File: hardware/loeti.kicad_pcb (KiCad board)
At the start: 2 copper layers, 69.3 x 41.9 mm, 64 parts, among them J1 GCT USB4105, J2 AudioJack3, J3 20021112-00014T1LF, Q1 BC817, Q2 BC817, Q3 BC807, Q4 Si4825DDY, DMG4435SSS, IRF939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, SW1 D6R, U1 STUSB4500QTR, U2 AP2204R-3.3, U3 STM32F030K6Tx, U4 74AHC1G08, U5 INA301, U6 TMP100, U7 TLV333-DBV

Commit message: two-temperature mode
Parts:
- removed D7: LED, LED_THT:LED_D1.8mm_W3.3mm_H2.4mm
- removed R12: 10k, Resistor_SMD:R_0603_1608Metric_Pad0.98x0.95mm_HandSolder
- C12, C13: value 100n -> DNP
- R10, R11, R18: value 10k -> 1k
- R13: value 1k -> 10k
- moved D6 7.04 mm to (83.0, -40.5), turned to 0 degrees
- moved D5 5.66 mm to (83.0, -43.5), turned to 0 degrees
- moved R11 5.64 mm to (84.0, -47.5), turned to 180 degrees
- moved R10 4.80 mm to (84.0, -45.8), turned to 180 degrees
- moved R3 1.25 mm to (84.5, -37.8), turned to 0 degrees
- moved R1 1.00 mm to (78.8, -39.5)
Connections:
- D5 pad 1: HEATER- -> Net-(D5-Pad1)
- D5 pad 2: Net-(D5-Pad2) -> LED0
- D6 pad 1: HEATER- -> Net-(D6-Pad1)
- D6 pad 2: Net-(D6-Pad2) -> LED1
- R10 pad 1: Net-(D5-Pad2) -> HEATER-
- R10 pad 2: LED0 -> Net-(D5-Pad1)
- R11 pad 1: Net-(D6-Pad2) -> HEATER-
- R11 pad 2: LED1 -> Net-(D6-Pad1)
- U3 pad 27: LED2 -> (no net)
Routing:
- net Net-(D6-Pad1): track 0.00 -> 9.67 mm
- net LED2: track 8.74 -> 0.00 mm
- net Net-(D7-Pad2): track 3.85 -> 0.00 mm
- net LED0: track 4.79 -> 7.56 mm
- net Net-(D6-Pad2): track 2.67 -> 0.00 mm
- net Net-(D5-Pad1): track 0.00 -> 2.54 mm
- net Net-(D5-Pad2): track 2.05 -> 0.00 mm
- net HEATER-: track 65.7 -> 67.5 mm, vias 66 -> 67
- net LED1: track 6.95 -> 5.99 mm
- net SHUNT+: track 58.7 -> 57.8 mm
- net NRST: track 23.0 -> 22.2 mm, vias 2 -> 1
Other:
- board text added: "af 2021 v5b"
- board text removed: "af 2021 v5"

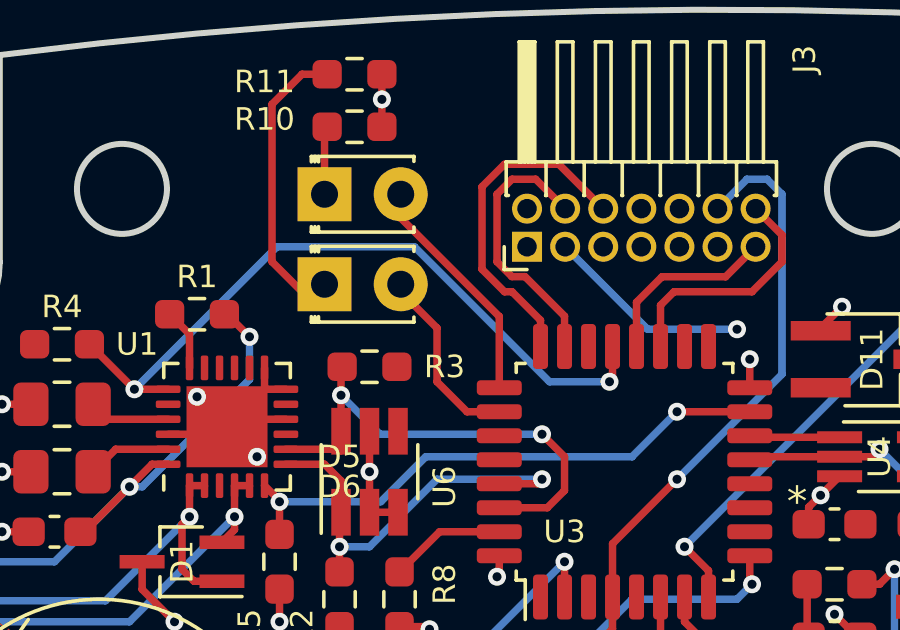
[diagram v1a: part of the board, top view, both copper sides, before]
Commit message: improved display v5b complete
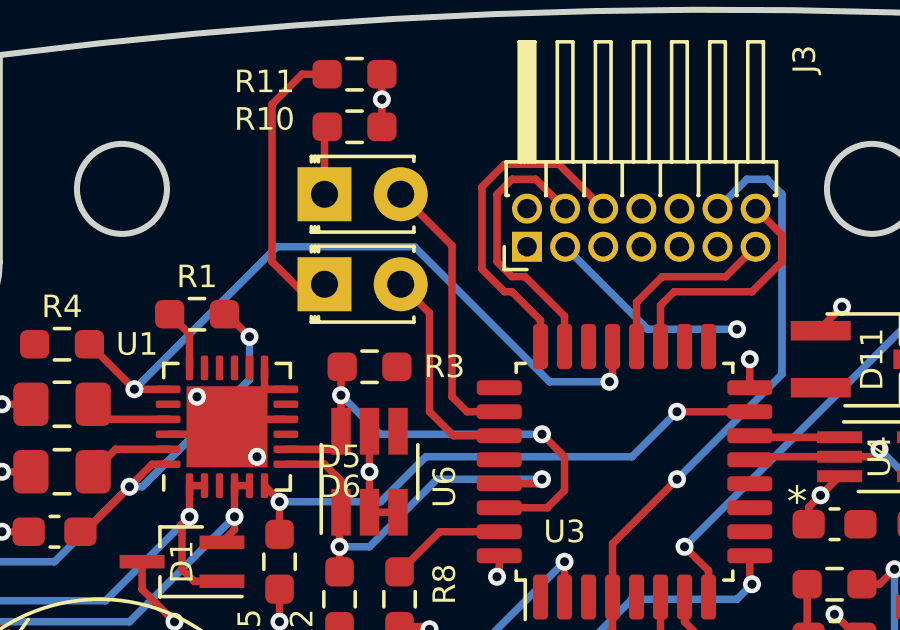
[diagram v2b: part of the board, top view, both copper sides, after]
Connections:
- D5 pad 2: LED0 -> LED1
- D6 pad 2: LED1 -> LED2
- U3 pad 25: LED0 -> (no net)
- U3 pad 27: (no net) -> LED2
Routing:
- net LED0: track 7.56 -> 0.00 mm
- net LED2: track 0.00 -> 7.30 mm
- net LED1: track 5.99 -> 9.24 mm

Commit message: initiali loeti tiny
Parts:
- C10, C11, C12, C13, C14, C6, C8, C9: footprint Capacitor_SMD:C_0603_1608Metric_Pad1.08x0.95mm_HandSolder -> Capacitor_SMD:C_0603_1608Metric
- C3, C4, C5, C7: footprint Capacitor_SMD:C_0805_2012Metric_Pad1.18x1.45mm_HandSolder -> Capacitor_SMD:C_0805_2012Metric
- D1, D3, D4, D8, D9: footprint Package_TO_SOT_SMD:SOT-323_SC-70_Handsoldering -> Package_TO_SOT_SMD:SOT-323_SC-70
- D11: footprint Package_TO_SOT_SMD:TSOT-23_HandSoldering -> Package_TO_SOT_SMD:TSOT-23
- D2: footprint Diode_SMD:D_0603_1608Metric_Pad1.05x0.95mm_HandSolder -> Diode_SMD:D_0603_1608Metric
- D5: value LED -> LED_green
- D6: value LED -> LED_red
- Q1, Q2, Q3: footprint Package_TO_SOT_SMD:SOT-23_Handsoldering -> Package_TO_SOT_SMD:SOT-23
- R1, R10, R11, R13, R14, R15, R16, R17, R18, R2, R20, R21, R22, R23, R24, R3, R4, R5, R6, R7, R8, R9: footprint Resistor_SMD:R_0603_1608Metric_Pad0.98x0.95mm_HandSolder -> Resistor_SMD:R_0603_1608Metric
- R19: footprint Resistor_SMD:R_2010_5025Metric_Pad1.40x2.65mm_HandSolder -> Resistor_SMD:R_2010_5025Metric
- U2: footprint Package_TO_SOT_SMD:SOT-89-3_Handsoldering -> Package_TO_SOT_SMD:SOT-89-3
- U3: footprint Package_QFP:LQFP-32_7x7mm_P0.8mm -> Package_DFN_QFN:QFN-32-1EP_5x5mm_P0.5mm_EP3.1x3.1mm
- U4: footprint Package_TO_SOT_SMD:SOT-353_SC-70-5_Handsoldering -> Package_TO_SOT_SMD:SOT-353_SC-70-5
- U6: footprint Package_TO_SOT_SMD:SOT-23-6_Handsoldering -> Package_TO_SOT_SMD:SOT-23-6
- U7: footprint Package_TO_SOT_SMD:SOT-23-5_HandSoldering -> Package_TO_SOT_SMD:SOT-23-5

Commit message: feat: loeti v5
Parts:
- removed D11: BZX84Cxx, Package_TO_SOT_SMD:TSOT-23
- removed D8, D9: BAS16W, Package_TO_SOT_SMD:SOT-323_SC-70
- added C15: 1u, Capacitor_SMD:C_0603_1608Metric, F.Cu at (157.5, 113.1)
- added C16: 330p, Capacitor_SMD:C_0603_1608Metric, F.Cu at (132.8, 82.0)
- added C17: 1u, Capacitor_SMD:C_0603_1608Metric, F.Cu at (162.8, 113.9)
- added C18: 1u, Capacitor_SMD:C_0603_1608Metric, F.Cu at (167.8, 113.9)
- added C19: 1u, Capacitor_SMD:C_0603_1608Metric, F.Cu at (152.6, 113.1)
- added C20: 1u, Capacitor_SMD:C_0603_1608Metric, F.Cu at (154.2, 113.1)
- added C21: 100n, Capacitor_SMD:C_0603_1608Metric, F.Cu at (125.4, 83.5)
- added C22: 100n, Capacitor_SMD:C_0603_1608Metric, F.Cu at (158.2, 93.6)
- added C23: 100n, Capacitor_SMD:C_0603_1608Metric, F.Cu at (161.6, 91.8)
- added C24: 100n, Capacitor_SMD:C_0603_1608Metric, F.Cu at (154.5, 80.8)
- added C25: 100n, Capacitor_SMD:C_0603_1608Metric, F.Cu at (149.4, 92.4)
- added C26: 100n, Capacitor_SMD:C_0603_1608Metric, F.Cu at (150.4, 80.8)
- added C27: 1u, Capacitor_SMD:C_0603_1608Metric, F.Cu at (123.8, 77.1)
- added C28: 100n, Capacitor_SMD:C_0603_1608Metric, F.Cu at (158.2, 103.7)
- added C29: 1u, Capacitor_SMD:C_0603_1608Metric, F.Cu at (123.8, 78.8)
- added C30: 100n, Capacitor_SMD:C_0603_1608Metric, F.Cu at (165.1, 83.4)
- added C31: 100n, Capacitor_SMD:C_0603_1608Metric, F.Cu at (165.1, 80.2)
- added C32: 100n, Capacitor_SMD:C_0603_1608Metric, F.Cu at (171.2, 83.6)
- added D7: BZX84Cxx, Package_TO_SOT_SMD:TSOT-23_HandSoldering, F.Cu at (143.1, 105.5)
- added Q6: FDS6630A, Package_SO:SOIC-8_3.9x4.9mm_P1.27mm, F.Cu at (124.6, 89.4)
- added R12: 5.1k, Resistor_SMD:R_0603_1608Metric, F.Cu at (171.9, 95.8)
- added R25: 10k, Resistor_SMD:R_0603_1608Metric, F.Cu at (119.5, 114.9)
- added R26: 1k, Resistor_SMD:R_0603_1608Metric, F.Cu at (129.0, 111.6)
- added R27: TBD, Resistor_SMD:R_0603_1608Metric, F.Cu at (128.0, 78.9)
- added R28: 10k, Resistor_SMD:R_0603_1608Metric, F.Cu at (166.8, 83.4)
- added R29: 10k, Resistor_SMD:R_0603_1608Metric, F.Cu at (166.8, 80.2)
- added R30: 10k, Resistor_SMD:R_0603_1608Metric, F.Cu at (168.4, 80.2)
- added R31: 10k, Resistor_SMD:R_0603_1608Metric, F.Cu at (168.4, 83.4)
- added R32: 10k, Resistor_SMD:R_0603_1608Metric, F.Cu at (171.2, 86.9)
- added R33: 10k, Resistor_SMD:R_0603_1608Metric, F.Cu at (171.2, 85.2)
- added SW2: BOOT, Button_Switch_SMD:SW_SPST_TL3342, F.Cu at (175.7, 94.4)
- added TP1: SLEEP, TestPoint:TestPoint_THTPad_D2.0mm_Drill1.0mm, F.Cu at (183.8, 94.5)
- added U10: M24C64-RMN, Package_SO:SOIC-8_3.9x4.9mm_P1.27mm, F.Cu at (160.0, 99.8)
- added U8: AMS1117-3.3, Package_TO_SOT_SMD:SOT-223-3_TabPin2, F.Cu at (137.6, 104.1)
- added X2: SG-210STF (16 MHz), Oscillator:Oscillator_SMD_SeikoEpson_SG210-4Pin_2.5x2.0mm, F.Cu at (161.6, 89.0)
- C1: value CP -> 68u; footprint Capacitor_SMD:CP_Elec_6.3x5.9 -> Capacitor_THT:C_Radial_D10.0mm_H12.5mm_P5.00mm
- C10, C8: value 100n -> DNP
- C2: value CP -> 330p; footprint Capacitor_SMD:CP_Elec_6.3x5.9 -> Capacitor_SMD:C_0603_1608Metric
- C3, C4: value 1u -> 10u; footprint Capacitor_SMD:C_0805_2012Metric -> Capacitor_SMD:C_1206_3216Metric
- C5: value 4.7u -> 100n; footprint Capacitor_SMD:C_0805_2012Metric -> Capacitor_SMD:C_0603_1608Metric
- C7: value 4.7u -> 1u; footprint Capacitor_SMD:C_0805_2012Metric -> Capacitor_SMD:C_0603_1608Metric
- D1: value ESDA25W -> BAT54S; footprint Package_TO_SOT_SMD:SOT-323_SC-70 -> Package_TO_SOT_SMD:SOT-23
- D10: value D_Schottky -> B5819W SL
- D2: value ESDA25P35 -> BAT54S; footprint Diode_SMD:D_0603_1608Metric -> Package_TO_SOT_SMD:SOT-23
- D3, D4: value BAS16W -> BAT54S; footprint Package_TO_SOT_SMD:SOT-323_SC-70 -> Package_TO_SOT_SMD:SOT-23
- D5: value LED_green -> ESDA25P35-1U1M; footprint LED_THT:LED_D1.8mm_W3.3mm_H2.4mm -> Diode_SMD:ST_QFN-2L_1.6x1.0mm
- D6: value LED_red -> BAT54S; footprint LED_THT:LED_D1.8mm_W3.3mm_H2.4mm -> Package_TO_SOT_SMD:SOT-23
- J1: value GCT USB4105 -> REDFIT_SWD_6; footprint Connector_USB:USB_C_Receptacle_HRO_TYPE-C-31-M-12 -> connectors-debug:WR-WST REDFIT IDC 6 DBG
- J3: value 20021112-00014T1LF -> USB_C_Receptacle_USB2.0; footprint Connector_PinHeader_1.27mm:PinHeader_2x07_P1.27mm_Horizontal -> Connector_USB:USB_C_Receptacle_G-Switch_GT-USB-7010ASV
- Q4: value Si4825DDY, DMG4435SSS, IRF9393PbF -> Si4425FDY
- R1, R2: value 1k -> 33
- R10: value 1k -> 10k
- R11: value 1k -> 1M
- R20: value 20 -> 0.47
- R3: value 1k -> 5.1k
- R4: value 1k -> 220k
- R5, R8: value 10k -> 5.1k
- SW1: value D6R -> RotaryEncoder_Switch; footprint custom:D6R -> Rotary_Encoder:RotaryEncoder_Bourns_Horizontal_PEC09-2xxxF-Sxxxx
- U1: value STUSB4500QTR -> STM32G431C_6-8-B_Tx; footprint Package_DFN_QFN:QFN-24-1EP_4x4mm_P0.5mm_EP2.7x2.7mm -> Package_QFP:LQFP-48_7x7mm_P0.5mm
- U2: value AP2204R-3.3 -> EA_OLEDS102-6; footprint Package_TO_SOT_SMD:SOT-89-3 -> display-visions:EA_OLEDS102-6; moved to B.Cu
- U3: value STM32F030K6Tx -> USBLC6-2SC6; footprint Package_DFN_QFN:QFN-32-1EP_5x5mm_P0.5mm_EP3.1x3.1mm -> Package_TO_SOT_SMD:SOT-23-6
- U5: footprint Package_SO:VSSOP-8_3.0x3.0mm_P0.65mm -> Package_SO:VSSOP-8_3x3mm_P0.65mm
- U6: value TMP100 -> Opamp_Dual; footprint Package_TO_SOT_SMD:SOT-23-6 -> Package_SO:VSSOP-8_3x3mm_P0.65mm
- U7: value TLV333-DBV -> ~; footprint Package_TO_SOT_SMD:SOT-23-5 -> Package_DFN_QFN:QFN-12-1EP_3x3mm_P0.51mm_EP1.45x1.45mm
- moved J1 182.3 mm to (175.6, 109.1)
- moved C5 176.4 mm to (159.1, 113.1), turned to -90 degrees
- moved C7 170.7 mm to (155.9, 113.1)
- moved R11 167.8 mm to (119.5, 116.5)
- moved R10 166.6 mm to (181.1, 89.6), turned to 90 degrees
- moved C6 163.5 mm to (148.8, 113.1), turned to -90 degrees
- moved R4 158.7 mm to (125.8, 111.6), turned to 90 degrees
- moved U2 157.1 mm to (152.6, 96.8), turned to -90 degrees
- moved D1 153.0 mm to (123.1, 115.0)
- moved R3 152.7 mm to (158.2, 96.0)
- moved SW1 152.2 mm to (181.9, 84.9), turned to 0 degrees
- moved D3 150.8 mm to (183.8, 89.8)
- moved U6 149.2 mm to (123.0, 109.9), turned to -90 degrees
- moved D6 148.8 mm to (141.0, 96.5), turned to 90 degrees
- moved C3 148.7 mm to (136.8, 98.4)
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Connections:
- net SHUNT- renamed /SHUNT-
- C1 pad 1: SHUNT+ -> VDC
- C1 pad 2: HEATER- -> GND
- C10 pad 1: +3V3 -> /TEMP_245
- C10 pad 2: HEATER- -> Net-(U6B--)
- C11 pad 1: ADC_IN1 -> /CURR_OUT
- C11 pad 2: HEATER- -> GND
- C12 pad 1: T+ -> /HEATER/245
- C12 pad 2: HEATER- -> GND
- C13 pad 1: Net-(C13-Pad1) -> /TEMP_210
- C13 pad 2: Net-(C13-Pad2) -> Net-(U6A--)
- C14 pad 2: HEATER- -> GND
- C2 pad 1: SHUNT+ -> /UCPD_CC2
- C2 pad 2: HEATER- -> GND
- C3 pad 1: HEATER- -> VDC
- C3 pad 2: Net-(C3-Pad2) -> GND
- C4 pad 1: Net-(C4-Pad1) -> VDC
- C4 pad 2: HEATER- -> GND
- C5 pad 1: SHUNT+ -> GND
- C5 pad 2: HEATER- -> +3V3
- C6 pad 1: HEATER- -> GND
- C6 pad 2: SHUNT+ -> +3V3
- C7 pad 1: +3V3 -> GND
- C7 pad 2: HEATER- -> /OLED_VCC
- C8 pad 1: +3V3 -> /DETECT/210
- C8 pad 2: HEATER- -> GND
- C9 pad 2: HEATER- -> GND
- D1 pad 1: CC1 -> GND
- D1 pad 2: CC2 -> +3V3
- D1 pad 3: HEATER- -> Net-(D1-COM)
- D10 pad 1: HEATER+ -> /HEATER/245
- D10 pad 2: HEATER- -> GND
- D2 pad 1: SHUNT+ -> GND
- D2 pad 2: HEATER- -> +3V3
- D3 pad 1: ADC_IN3 -> GND
- D3 pad 2: (no net) -> +3V3
- D3 pad 3: +3V3 -> Net-(D3-COM)
- D4 pad 1: HEATER- -> VBUS
- D4 pad 2: (no net) -> unconnected-(D4-K-Pad2)
- D4 pad 3: ADC_IN3 -> Net-(D4-COM)
- D5 pad 1: Net-(D5-Pad1) -> VBUS
- D5 pad 2: LED1 -> GND
- D6 pad 1: Net-(D6-Pad1) -> GND
- D6 pad 2: LED2 -> +3V3
- J2 pad R: T+ -> /DETECT/210
- J2 pad S: HEATER- -> GND
- J2 pad T: HEATER+ -> /HEATER/245
- Q1 pad 2: HEATER- -> GND
- Q2 pad 3: SHUNT+ -> VDC
- Q3 pad 3: HEATER- -> GND
- Q4 pad 5: HEATER+ -> /HEATER/245
- Q4 pad 6: HEATER+ -> /HEATER/245
- Q4 pad 7: HEATER+ -> /HEATER/245
- Q4 pad 8: HEATER+ -> /HEATER/245
- R1 pad 1: Net-(R1-Pad1) -> /_USB_D_N
- R1 pad 2: SHUNT+ -> /USB_D_N
- R10 pad 1: HEATER- -> Net-(R10-Pad1)
- R10 pad 2: Net-(D5-Pad1) -> Net-(D3-COM)
- R11 pad 1: HEATER- -> +3V3
- R11 pad 2: Net-(D6-Pad1) -> /DETECT/210
- R13 pad 1: ADC_IN1 -> /CURR_OUT
- R14 pad 1: HEATER- -> GND
- R14 pad 2: Net-(R14-Pad2) -> /DAC1_OUT1
- R16 pad 2: T+ -> /HEATER/245
- R17 pad 1: T+ -> Net-(D2-COM)
- R17 pad 2: Net-(D8-Pad1) -> /HEATER/245
- R18 pad 2: SHUNT+ -> VDC
- R19 pad 1: SHUNT+ -> VDC
- R2 pad 1: I2C1_SCL -> /_USB_D_P
- R2 pad 2: +3V3 -> /USB_D_P
- R21 pad 1: Net-(C13-Pad1) -> /TEMP_210
- R21 pad 2: Net-(C13-Pad2) -> Net-(U6A--)
- R22 pad 1: Net-(C13-Pad2) -> Net-(U6A--)
- R22 pad 2: HEATER- -> GND
- R23 pad 1: ADC_IN2 -> Net-(U7-VBUS_CTRL)
- R23 pad 2: Net-(C13-Pad1) -> VBUS
- R24 pad 1: CURR_ALERT -> /CURR_ALERT
- R3 pad 1: I2C1_SDA -> /I2C1_SDA
- R4 pad 1: PD_ALERT_INT -> /TEMP_245
- R4 pad 2: +3V3 -> Net-(U6B--)
- R5 pad 1: HEATER- -> +3V3
- R5 pad 2: PD_RST -> /NRST
- R6 pad 1: ADC_IN3 -> /ADC2_IN3
- R6 pad 2: SHUNT+ -> VDC
- R7 pad 1: HEATER- -> GND
- R7 pad 2: ADC_IN3 -> /ADC2_IN3
- R8 pad 1: HEATER- -> /I2C1_SCL
- R8 pad 2: BOOT0 -> +3V3
- R9 pad 1: +3V3 -> Net-(U7-~{FLT})
- R9 pad 2: NRST -> +3V3
- U1 pad 1: CC1 -> +3V3
- U1 pad 10: HEATER- -> /ROT_A
- U1 pad 11: (no net) -> /ROT_B
- U1 pad 12: HEATER- -> /DAC1_OUT1
- U1 pad 13: HEATER- -> unconnected-(U1-PA5-Pad13)
- U1 pad 14: (no net) -> /ADC2_IN3
- U1 pad 15: (no net) -> unconnected-(U1-PA7-Pad15)
- U1 pad 16: (no net) -> unconnected-(U1-PB0-Pad16)
- U1 pad 17: (no net) -> unconnected-(U1-PB1-Pad17)
- U1 pad 18: Net-(R1-Pad1) -> unconnected-(U1-PB2-Pad18)
- U1 pad 19: PD_ALERT_INT -> GND
- U1 pad 2: CC1 -> unconnected-(U1-PC13-Pad2)
- U1 pad 20: (no net) -> unconnected-(U1-VREF+-Pad20)
- U1 pad 21: Net-(C3-Pad2) -> +3V3
- U1 pad 22: HEATER- -> /CURR_ALERT
- U1 pad 23: Net-(C4-Pad1) -> GND
- U1 pad 24: SHUNT+ -> +3V3
- U1 pad 25: HEATER- -> /TIM2_CH4
- U1 pad 3: (no net) -> unconnected-(U1-PC14-Pad3)
- U1 pad 4: CC2 -> unconnected-(U1-PC15-Pad4)
- U1 pad 5: CC2 -> Net-(U1-PF0)
- U1 pad 6: PD_RST -> unconnected-(U1-PF1-Pad6)
- U1 pad 7: I2C1_SCL -> /NRST
- U1 pad 8: I2C1_SDA -> Net-(D3-COM)
- U1 pad 9: (no net) -> /ROT_SW
- U2 pad 1: SHUNT+ -> /SPI2_SCK
- U2 pad 2: HEATER- -> /SPI2_MOSI
- U2 pad 3: +3V3 -> /SPI2_MISO
- U3 pad 1: +3V3 -> Net-(J3-D--PadA7)
- U3 pad 2: SW -> GND
- U3 pad 3: (no net) -> Net-(J3-D+-PadA6)
- U3 pad 4: NRST -> /_USB_D_P
- U3 pad 5: +3V3 -> VBUS
- U3 pad 6: CURR_RESET -> /_USB_D_N
- U4 pad 1: PWM -> /TIM2_CH4
- U4 pad 2: CURR_ALERT -> /CURR_ALERT
- U4 pad 3: HEATER- -> GND
- U5 pad 3: Net-(R14-Pad2) -> /DAC1_OUT1
- U5 pad 4: HEATER- -> GND
- U5 pad 5: CURR_RESET -> /CURR_RESET
- U5 pad 6: CURR_ALERT -> /CURR_ALERT
- U5 pad 8: SHUNT+ -> VDC
- U6 pad 1: I2C1_SCL -> /TEMP_210
- U6 pad 2: HEATER- -> Net-(U6A--)
- U6 pad 3: HEATER- -> Net-(D2-COM)
- U6 pad 4: +3V3 -> GND
- U6 pad 5: HEATER- -> Net-(D1-COM)
- U6 pad 6: I2C1_SDA -> Net-(U6B--)
- U7 pad 1: Net-(C13-Pad1) -> /UCPD_CC2
- U7 pad 2: HEATER- -> GND
- U7 pad 3: Net-(D8-Pad1) -> /UCPD_CC1
- U7 pad 4: Net-(C13-Pad2) -> VDC
- U7 pad 5: +3V3 -> Net-(Q6-G)
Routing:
- net HEATER-: track 67.5 -> 0.00 mm, vias 67 -> 0
- net +3V3: track 12.9 -> 72.5 mm, vias 1 -> 26
- net SHUNT+: track 57.8 -> 0.00 mm, vias 5 -> 0
- net /CURR_ALERT: track 0.00 -> 50.1 mm, vias 0 -> 2
- net /DAC1_OUT1: track 0.00 -> 49.1 mm, vias 0 -> 2
- net VDC: track 0.00 -> 46.9 mm, vias 0 -> 3
- net /NRST: track 0.00 -> 42.9 mm
- net /TIM2_CH4: track 0.00 -> 39.6 mm, vias 0 -> 2
- net /CURR_RESET: track 0.00 -> 39.2 mm, vias 0 -> 2
- net /SPI2_NSS: track 0.00 -> 37.6 mm, vias 0 -> 1
- net /TMS: track 0.00 -> 36.5 mm
- net /OLED_NRST: track 0.00 -> 35.6 mm, vias 0 -> 1
- net /OLED_D_C: track 0.00 -> 35.4 mm, vias 0 -> 1
- net /TCK: track 0.00 -> 34.7 mm
- net /UCPD_CC1: track 0.00 -> 33.8 mm, vias 0 -> 2
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- added copper zone on In2.Cu, net +3V3
- added copper zone on F.Cu, net /HEATER/245
- added copper zone on B.Cu, net GND
- added copper zone on F.Cu, net GND
- added copper zone on In1.Cu, net GND
- added copper zone on F.Cu, net VBUS
- added copper zone on F.Cu, net VDC
- removed copper zone on F.Cu, net +3V3
- removed copper zone on F.Cu, net HEATER+
- removed copper zone on B.Cu, net HEATER-
- removed copper zone on F.Cu, net HEATER-
- removed copper zone on F.Cu, net SHUNT+
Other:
- board size 69.3 x 41.9 mm -> 80 x 50.5 mm
- copper layers 2 -> 4
- net class Default removed
- board text added: "af 24 rev a"
- board text removed: "af 2021 v5b"

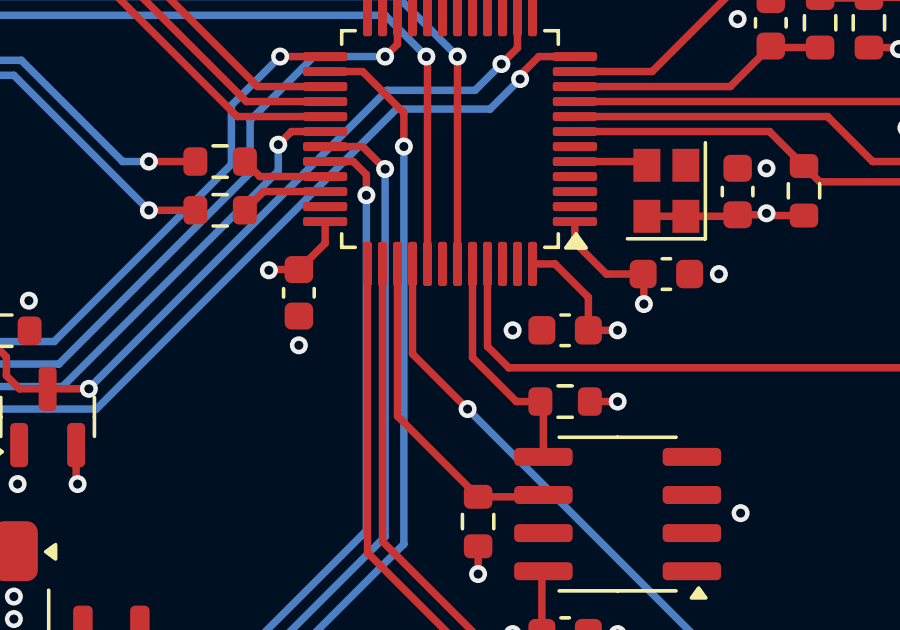
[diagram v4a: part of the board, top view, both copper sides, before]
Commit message: feat: initial display implementation
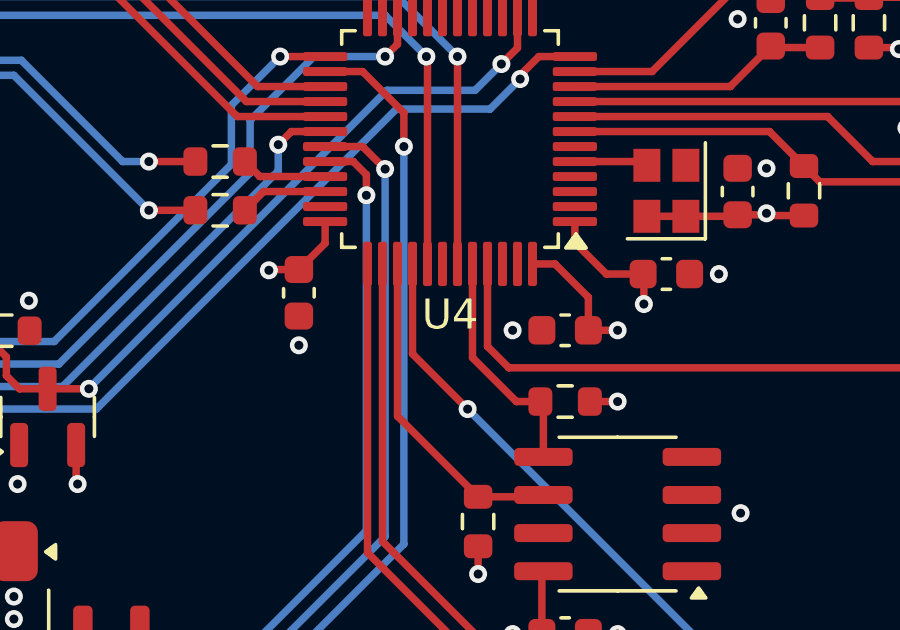
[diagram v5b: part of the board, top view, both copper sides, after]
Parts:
- removed the U1 at (154.4, 87.2)
- added U4: STM32G431CBTx, Package_QFP:LQFP-48_7x7mm_P0.5mm, F.Cu at (154.4, 87.2)
- renumbered C28 to C1, C20 to C10, C29 to C11, C27 to C12, C1 to C13, C22 to C14, C23 to C15, C24 to C16, C25 to C17, C26 to C18, C3 to C19, C7 to C2, C4 to C20, C30 to C21, C31 to C22, C32 to C23, C21 to C24, C12 to C25, C13 to C26, C2 to C27, C16 to C28, C8 to C29, C15 to C3, C14 to C30, C10 to C31, C11 to C32, C5 to C4, C6 to C5, C9 to C6, C17 to C7, C18 to C8, C19 to C9, D3 to D1, D6 to D2, D7 to D3, D5 to D4, D2 to D5, D4 to D6, D10 to D7, D1 to D8, J3 to J2, J2 to J3, Q2 to Q1, Q6 to Q2, Q4 to Q3, Q1 to Q4, Q3 to Q5, R10 to R1, R30 to R10, R31 to R11, R32 to R12, R28 to R13, R33 to R14, R29 to R15, R18 to R16, R20 to R17, R15 to R18, R16 to R19, R1 to R2, R23 to R20, R17 to R21, R21 to R22, R9 to R23, R27 to R24, R22 to R25, R11 to R26, R25 to R27, R19 to R28, R13 to R29, R2 to R3, R24 to R30, R4 to R31, R14 to R32, R26 to R33, R8 to R4, R3 to R6, R12 to R7, R6 to R8, R7 to R9, SW2 to SW1, SW1 to SW2, U3 to U1, U10 to U3, U8 to U5, U4 to U6, U6 to U7, U7 to U8, U5 to U9, X2 to X1

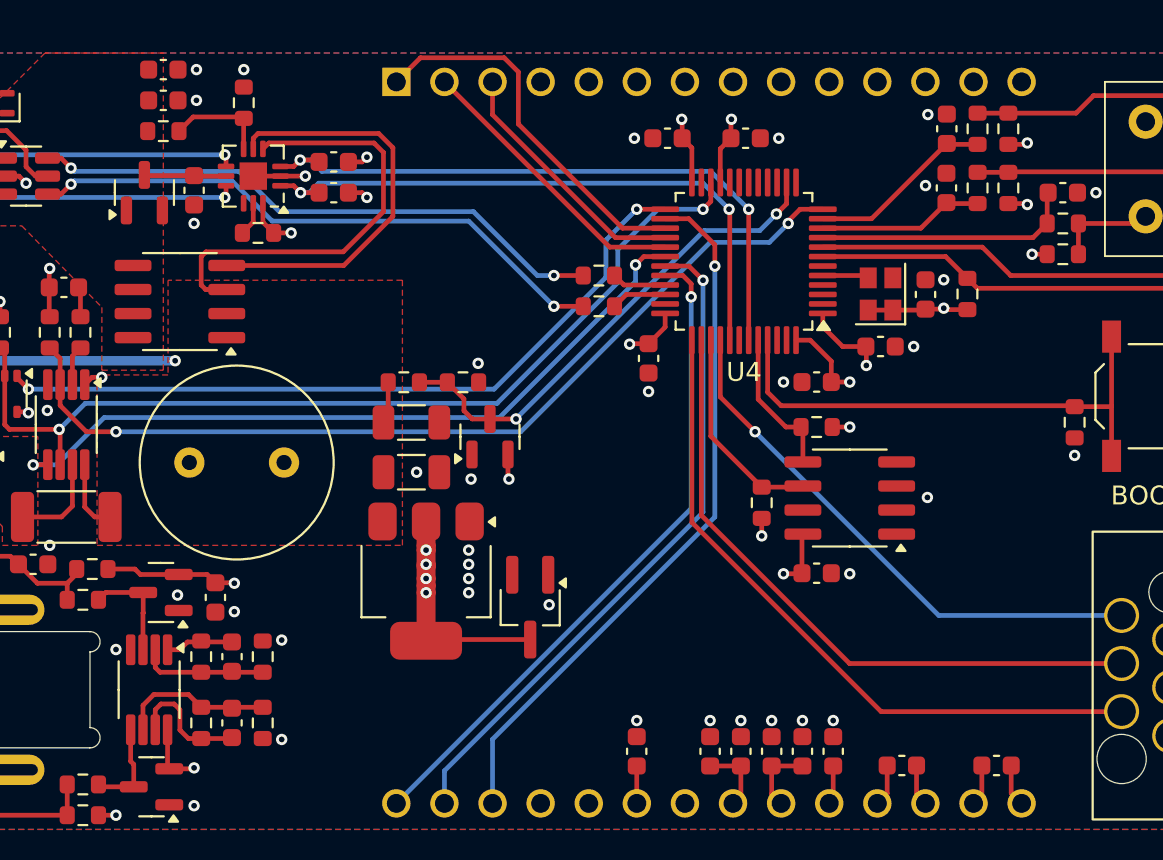
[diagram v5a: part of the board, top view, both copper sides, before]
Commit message: feat: enable dac
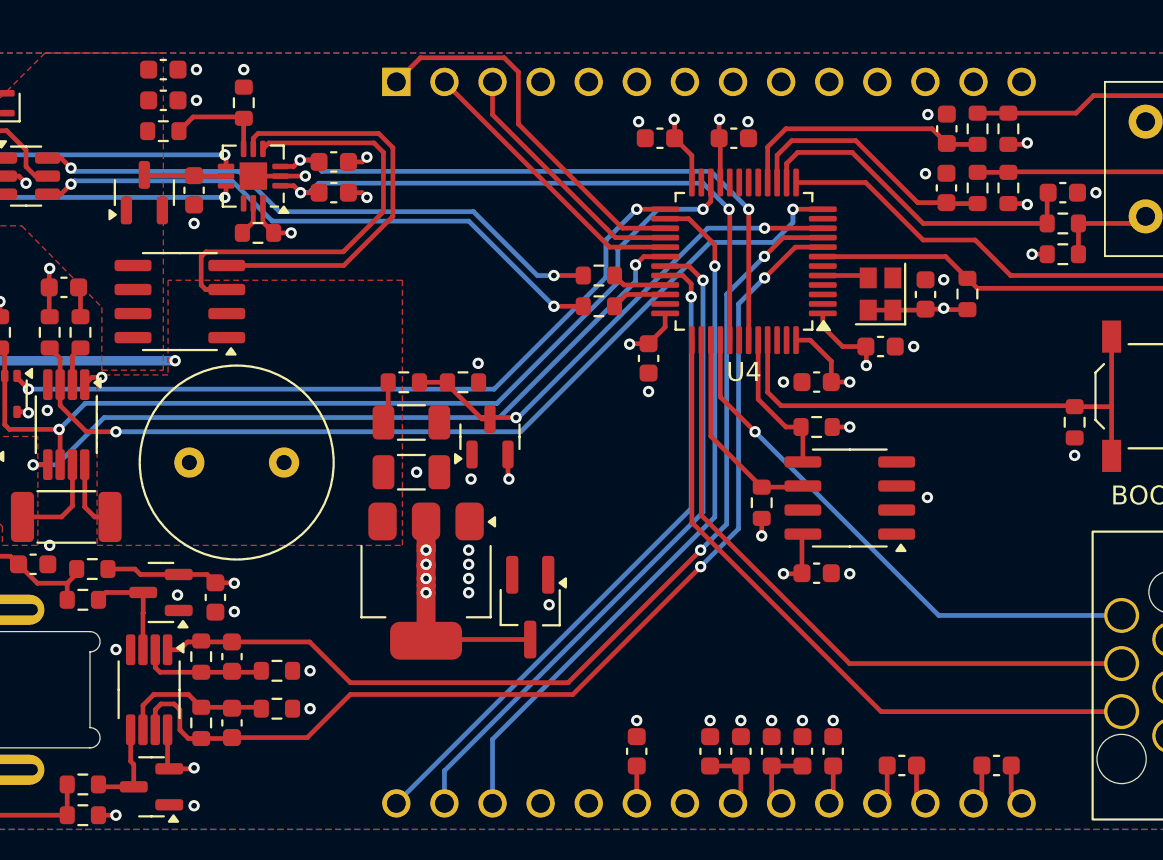
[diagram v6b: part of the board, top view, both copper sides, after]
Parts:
- moved R25 1.06 mm to (129.8, 108.9), turned to 0 degrees
- moved R33 1.06 mm to (129.8, 110.9), turned to 0 degrees
- moved C16 0.62 mm to (153.9, 80.8)
- moved C18 0.40 mm to (150.0, 80.8)
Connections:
- C26 pad 1: /TEMP_210 -> /ADC2_IN2
- C31 pad 1: /TEMP_245 -> /ADC2_IN1
- D1 pad 3: Net-(D1-COM) -> /SLEEP
- R1 pad 2: Net-(D1-COM) -> /SLEEP
- R22 pad 1: /TEMP_210 -> /ADC2_IN2
- R31 pad 1: /TEMP_245 -> /ADC2_IN1
- U4 pad 10: /ROT_A -> /ADC2_IN3
- U4 pad 11: /ROT_B -> unconnected-(U4-PA3-Pad11)
- U4 pad 13: unconnected-(U4-PA5-Pad13) -> /SLEEP
- U4 pad 14: /ADC2_IN3 -> /ROT_SW
- U4 pad 15: unconnected-(U4-PA7-Pad15) -> /ROT_A
- U4 pad 16: unconnected-(U4-PB0-Pad16) -> /ROT_B
- U4 pad 8: Net-(D1-COM) -> /ADC2_IN1
- U4 pad 9: /ROT_SW -> /ADC2_IN2
- U7 pad 1: /TEMP_210 -> /ADC2_IN2
- U7 pad 7: /TEMP_245 -> /ADC2_IN1
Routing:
- net /ADC2_IN1: track 0.00 -> 55.5 mm, vias 0 -> 2
- net /ADC2_IN2: track 0.00 -> 52.5 mm, vias 0 -> 2
- net /SLEEP: track 0.00 -> 28.9 mm
- net Net-(D1-COM): track 26.1 -> 0.00 mm
- net /TEMP_245: track 6.57 -> 0.00 mm
- net /ROT_A: track 8.68 -> 13.7 mm
- net /ROT_SW: track 13.7 -> 18.1 mm
- net /ROT_B: track 9.77 -> 13.6 mm
- net /TEMP_210: track 3.57 -> 0.00 mm
